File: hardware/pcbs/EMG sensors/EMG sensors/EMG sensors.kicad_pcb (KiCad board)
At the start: 4 copper layers, 65 x 26 mm, 29 parts, among them IC1 INA128, J1 Conn_01x04_Pin, J2 Conn_01x01_Pin, U6 OPA2188AIDR, U7 OPA188AIDR

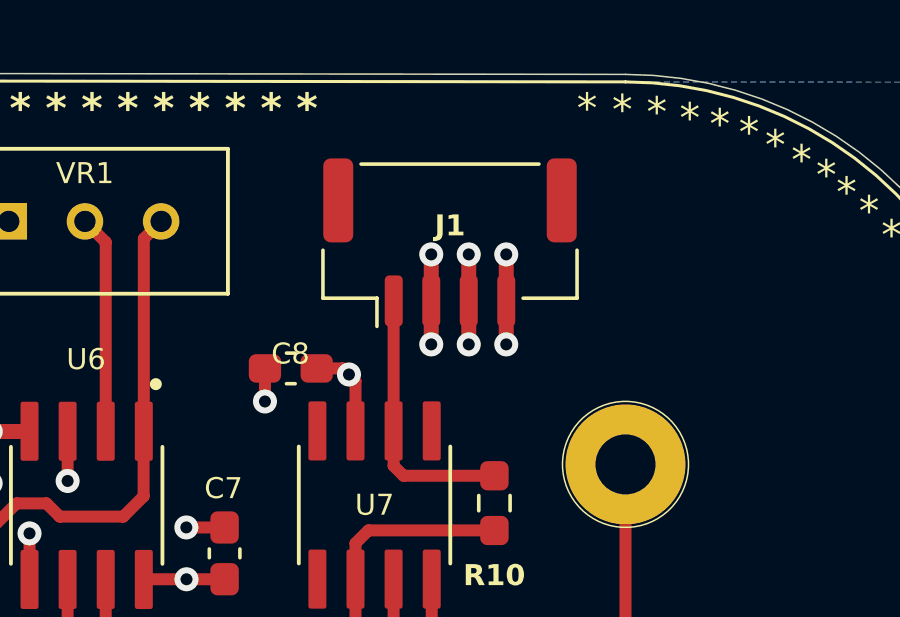
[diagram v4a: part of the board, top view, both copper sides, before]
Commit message: Connector update of the sEMG sensor
Changed it to be JST_GH_SM04B instead of JST_GH_BM04B for easier use
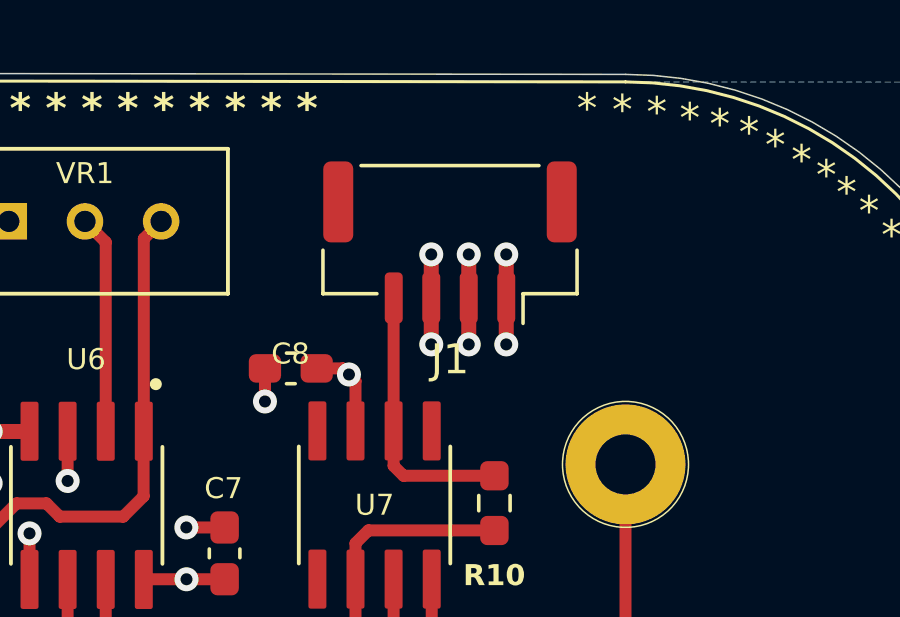
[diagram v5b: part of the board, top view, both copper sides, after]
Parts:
- J1: footprint Connector_JST:JST_GH_BM04B-GHS-TBT_1x04-1MP_P1.25mm_Vertical -> Connector_JST:JST_GH_SM04B-GHS-TB_1x04-1MP_P1.25mm_Horizontal
- turned J1 to 180 degrees
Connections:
- J1 pad 1: /AEMG -> /+5.5V
- J1 pad 2: GND -> /-5.5V
- J1 pad 3: /-5.5V -> GND
- J1 pad 4: /+5.5V -> /AEMG
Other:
- board text added: "v0.3"
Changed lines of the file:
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@@
 		)
 	)
-	(footprint "Connector_JST:JST_GH_BM04B-GHS-TBT_1x04-1MP_P1.25mm_Vertical"
+	(footprint "Connector_JST:JST_GH_SM04B-GHS-TB_1x04-1MP_P1.25mm_Horizontal"
 		(layer "F.Cu")
-		(at 145.15 103.2)
-		(descr "JST GH series connector, BM04B-GHS-TBT (http://www.jst-mfg.com/product/pdf/eng/eGH.pdf), generated with kicad-footprint-generator")
-		(tags "connector JST GH vertical")
+		(at 145.15 103.2 180)
+		(descr "JST GH series connector, SM04B-GHS-TB (http://www.jst-mfg.com/product/pdf/eng/eGH.pdf), generated with kicad-footprint-generator")
+		(tags "connector JST GH horizontal")
 		(property "Reference" "J1"
-			(at 0 -0.55845 180)
+			(at 0 -3.9 0)
 			(layer "F.SilkS")
 			(effects
 				(font
-					(size 0.7 0.7)
-					(thickness 0.12)
-					(bold yes)
+					(size 1 1)
+					(thickness 0.15)
 				)
 			)
 		)
 		(property "Value" "Conn_01x04_Pin"
-			(at 0 4 180)
+			(at 0 3.9 0)
 			(layer "F.Fab")
-			(hide yes)
 			(effects
 				(font
@@
 		)
 		(property "Datasheet" "~"
-			(at 0 0 180)
+			(at 0 0 0)
 			(layer "F.Fab")
 			(hide yes)
@@
 		)
 		(property "Description" "Generic connector, single row, 01x04, script generated"
-			(at 0 0 180)
+			(at 0 0 0)
 			(layer "F.Fab")
 			(hide yes)
@@
 		(attr smd)
 		(fp_line
-			(start -4.235 0.26)
-			(end -4.235 1.86)
+			(start 4.235 -0.26)
+			(end 4.235 -1.71)
 			(stroke
 				(width 0.12)
@@
 		)
 		(fp_line
-			(start -4.235 1.86)
-			(end -2.435 1.86)
+			(start 4.235 -1.71)
+			(end 2.435 -1.71)
 			(stroke
 				(width 0.12)
@@
 		)
 		(fp_line
-			(start -2.965 -2.61)
-			(end 2.965 -2.61)
+			(start -2.435 -1.71)
+			(end -2.435 -2.7)
 			(stroke
 				(width 0.12)
@@
 		)
 		(fp_line
-			(start -2.435 1.86)
-			(end -2.435 2.8)
+			(start -2.965 2.56)
+			(end 2.965 2.56)
 			(stroke
 				(width 0.12)
@@
 		)
 		(fp_line
-			(start 4.235 0.26)
-			(end 4.235 1.86)
+			(start -4.235 -0.26)
+			(end -4.235 -1.71)
 			(stroke
 				(width 0.12)
@@
 		)
 		(fp_line
-			(start 4.235 1.86)
-			(end 2.435 1.86)
+			(start -4.235 -1.71)
+			(end -2.435 -1.71)
 			(stroke
 				(width 0.12)
@@
 		)
 		(fp_line
-			(start -4.73 -3.3)
-			(end -2.72 -3.3)
+			(start 4.73 3.2)
+			(end 2.72 3.2)
 			(stroke
 				(width 0.05)
@@
 		)
 		(fp_line
-			(start -4.73 0.5)
-			(end -4.73 -3.3)
+			(start 4.73 -0.5)
+			(end 4.73 3.2)
 			(stroke
 				(width 0.05)
@@
 		)
 		(fp_line
-			(start -4.63 0.5)
-			(end -4.73 0.5)
+			(start 4.63 -0.5)
+			(end 4.73 -0.5)
 			(stroke
 				(width 0.05)
@@
 		)
 		(fp_line
-			(start -4.63 2.25)
-			(end -4.63 0.5)
+			(start 4.63 -2.1)
+			(end 4.63 -0.5)
 			(stroke
 				(width 0.05)
@@
 		)
 		(fp_line
-			(start -2.72 -3.3)
-			(end -2.72 -3)
+			(start 2.72 3.2)
+			(end 2.72 2.95)
 			(stroke
 				(width 0.05)
@@
 		)
 		(fp_line
-			(start -2.72 -3)
-			(end 2.719999 -3)
+			(start 2.72 2.95)
+			(end -2.72 2.95)
 			(stroke
 				(width 0.05)
@@
 		)
 		(fp_line
-			(start -2.680001 2.25)
-			(end -4.63 2.25)
+			(start 2.68 -2.1)
+			(end 4.63 -2.1)
 			(stroke
 				(width 0.05)
@@
 		)
 		(fp_line
-			(start -2.68 3.3)
-			(end -2.680001 2.25)
+			(start 2.68 -3.2)
+			(end 2.68 -2.1)
 			(stroke
 				(width 0.05)
@@
 		)
 		(fp_line
-			(start 2.68 2.250001)
-			(end 2.68 3.3)
+			(start -2.68 -2.1)
+			(end -2.68 -3.2)
 			(stroke
 				(width 0.05)
@@
 		)
 		(fp_line
-			(start 2.68 3.3)
-			(end -2.68 3.3)
+			(start -2.68 -3.2)
+			(end 2.68 -3.2)
 			(stroke
 				(width 0.05)
@@
 		)
 		(fp_line
-			(start 2.719999 -3)
-			(end 2.72 -3.3)
+			(start -2.72 3.2)
+			(end -4.73 3.2)
 			(stroke
 				(width 0.05)
@@
 		)
 		(fp_line
-			(start 2.72 -3.3)
-			(end 4.73 -3.3)
+			(start -2.72 2.95)
+			(end -2.72 3.2)
 			(stroke
 				(width 0.05)
@@
 		)
 		(fp_line
-			(start 4.629999 0.5)
-			(end 4.63 2.25)
+			(start -4.63 -0.5)
+			(end -4.63 -2.1)
 			(stroke
 				(width 0.05)
@@
 		)
 		(fp_line
-			(start 4.63 2.25)
-			(end 2.68 2.250001)
+			(start -4.63 -2.1)
+			(end -2.68 -2.1)
 			(stroke
 				(width 0.05)
@@
 		)
 		(fp_line
-			(start 4.73 -3.3)
-			(end 4.73 0.5)
+			(start -4.73 3.2)
+			(end -4.73 -0.5)
 			(stroke
 				(width 0.05)
@@
 		)
 		(fp_line
-			(start 4.73 0.5)
-			(end 4.629999 0.5)
+			(start -4.73 -0.5)
+			(end -4.63 -0.5)
 			(stroke
 				(width 0.05)
@@
 		)
 		(fp_line
-			(start -4.125 -2.5)
-			(end 4.125 -2.5)
+			(start 4.125 -1.6)
+			(end 4.125 2.45)
 			(stroke
 				(width 0.1)
@@
 		)
 		(fp_line
-			(start -4.124999 1.75)
-			(end -4.125 -2.5)
+			(start -1.875 -0.892893)
+			(end -1.375 -1.6)
 			(stroke
 				(width 0.1)
@@
 		)
 		(fp_line
-			(start -4.124999 1.75)
-			(end 4.125 1.75)
+			(start -2.375 -1.6)
+			(end -1.875 -0.892893)
 			(stroke
 				(width 0.1)
@@
 		)
 		(fp_line
-			(start -2.375 1.75)
-			(end -1.875 1.042893)
+			(start -4.125 2.45)
+			(end 4.125 2.45)
 			(stroke
 				(width 0.1)
@@
 		)
 		(fp_line
-			(start -1.875 1.042893)
-			(end -1.375 1.75)
+			(start -4.125 -1.6)
+			(end 4.125 -1.6)
 			(stroke
 				(width 0.1)
@@
 		)
 		(fp_line
-			(start 4.125 1.75)
-			(end 4.125 -2.5)
+			(start -4.125 -1.6)
+			(end -4.125 2.45)
 			(stroke
 				(width 0.1)
@@
 			(layer "F.Fab")
 		)
-		(fp_poly
-			(pts
-				(xy -2.125 -0.5) (xy -1.625001 -0.5) (xy -1.625 0) (xy -2.125 0)
-			)
-			(stroke
-				(width 0.1)
-				(type solid)
-			)
-			(fill no)
-			(layer "F.Fab")
-		)
-		(fp_poly
-			(pts
-				(xy -0.875 -0.5) (xy -0.375001 -0.5) (xy -0.375 0) (xy -0.875 0)
-			)
-			(stroke
-				(width 0.1)
-				(type solid)
-			)
-			(fill no)
-			(layer "F.Fab")
-		)
-		(fp_poly
-			(pts
-				(xy 0.375 -0.5) (xy 0.875 -0.500001) (xy 0.875 0) (xy 0.375 0)
-			)
-			(stroke
-				(width 0.1)
-				(type solid)
-			)
-			(fill no)
+		(fp_text user "${REFERENCE}"
+			(at 0 0 0)
 			(layer "F.Fab")
-		)
-		(fp_poly
-			(pts
-				(xy 1.625 -0.5) (xy 2.125 -0.5) (xy 2.125 0) (xy 1.625 0)
-			)
-			(stroke
-				(width 0.1)
-				(type solid)
+			(effects
+				(font
+					(size 1 1)
+					(thickness 0.15)
+				)
 			)
-			(fill no)
-			(layer "F.Fab")
 		)
 		(pad "1" smd roundrect
-			(at -1.875 1.95)
+			(at -1.875 -1.85 180)
 			(size 0.6 1.7)
 			(layers "F.Cu" "F.Mask" "F.Paste")
 			(roundrect_rratio 0.25)
-			(net 12 "/AEMG")
+			(net 11 "/+5.5V")
 			(pinfunction "Pin_1")
 			(pintype "passive")
 		)
 		(pad "2" smd roundrect
-			(at -0.625 1.95)
+			(at -0.625 -1.85 180)
 			(size 0.6 1.7)
 			(layers "F.Cu" "F.Mask" "F.Paste")
 			(roundrect_rratio 0.25)
-			(net 18 "GND")
+			(net 10 "/-5.5V")
 			(pinfunction "Pin_2")
 			(pintype "passive")
 		)
 		(pad "3" smd roundrect
-			(at 0.625 1.95)
+			(at 0.625 -1.85 180)
 			(size 0.6 1.7)
 			(layers "F.Cu" "F.Mask" "F.Paste")
 			(roundrect_rratio 0.25)
-			(net 10 "/-5.5V")
+			(net 18 "GND")
 			(pinfunction "Pin_3")
 			(pintype "passive")
 		)
 		(pad "4" smd roundrect
-			(at 1.875 1.950001)
+			(at 1.875 -1.85 180)
 			(size 0.6 1.7)
 			(layers "F.Cu" "F.Mask" "F.Paste")
 			(roundrect_rratio 0.25)
-			(net 11 "/+5.5V")
+			(net 12 "/AEMG")
 			(pinfunction "Pin_4")
 			(pintype "passive")
 		)
 		(pad "MP" smd roundrect
-			(at -3.725 -1.4)
-			(size 1 2.8)
+			(at -3.725 1.35 180)
+			(size 1 2.7)
 			(layers "F.Cu" "F.Mask" "F.Paste")
 			(roundrect_rratio 0.25)
 		)
 		(pad "MP" smd roundrect
-			(at 3.725 -1.4)
-			(size 1 2.8)
+			(at 3.725 1.35 180)
+			(size 1 2.7)
 			(layers "F.Cu" "F.Mask" "F.Paste")
 			(roundrect_rratio 0.25)
 		)
 		(embedded_fonts no)
-		(model "${KICAD9_3DMODEL_DIR}/Connector_JST.3dshapes/JST_GH_BM04B-GHS-TBT_1x04-1MP_P1.25mm_Vertical.step"
+		(model "${KICAD9_3DMODEL_DIR}/Connector_JST.3dshapes/JST_GH_SM04B-GHS-TB_1x04-1MP_P1.25mm_Horizontal.step"
 			(offset
 				(xyz 0 0 0)
@@
 	)
 	(gr_text "SensaLimb sEMG"
-		(at 141.1 101.61475 0)
+		(at 141.1 101 0)
+		(layer "B.SilkS")
+		(effects
+			(font
+				(size 1.5 1.5)
+				(thickness 0.3)
+				(bold yes)
+			)
+			(justify left bottom mirror)
+		)
+	)
+	(gr_text "v0.3\n"
+		(at 134.2 121.6 0)
 		(layer "B.SilkS")
 		(effects
@@
 	)
 	(segment
-		(start 143.27 105.155)
-		(end 143.275 105.15)
+		(start 143.30695 109.44675)
+		(end 143.27 109.4837)
 		(width 0.4)
 		(layer "F.Cu")
@@
 	)
 	(segment
-		(start 143.30695 109.44675)
-		(end 143.27 109.4837)
+		(start 143.27 105.055)
+		(end 143.275 105.05)
 		(width 0.4)
 		(layer "F.Cu")
@@
 	(segment
 		(start 143.27 109.4837)
-		(end 143.27 105.155)
+		(end 143.27 105.055)
 		(width 0.4)
 		(layer "F.Cu")
@@
 		(width 0.4)
 		(layer "F.Cu")
-		(net 12)
-	)
-	(segment
-		(start 143.27 105.1965)
-		(end 143.23195 105.15845)
-		(width 0.4)
-		(layer "F.Cu")

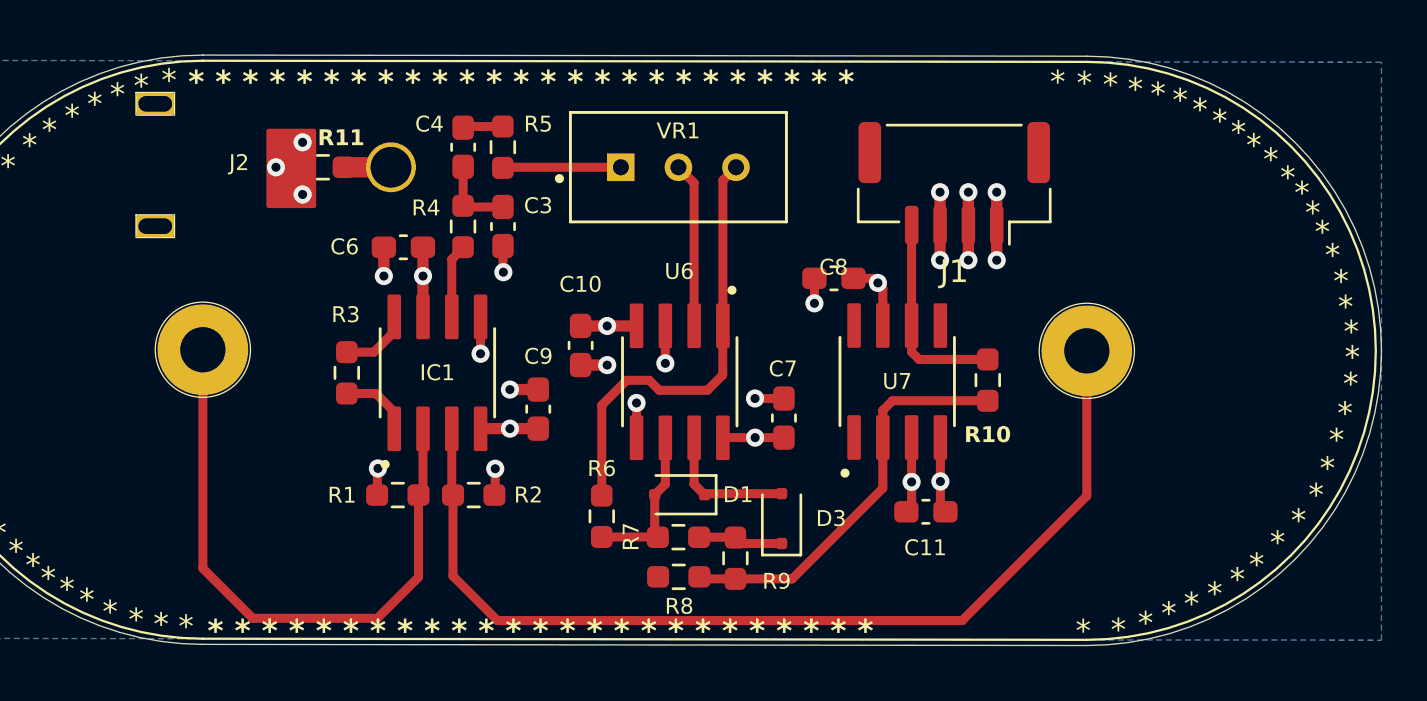
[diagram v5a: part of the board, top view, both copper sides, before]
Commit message: ADC + sEMG changes
sEMG - connector updates
ADC - major changes - connectors, layout changes
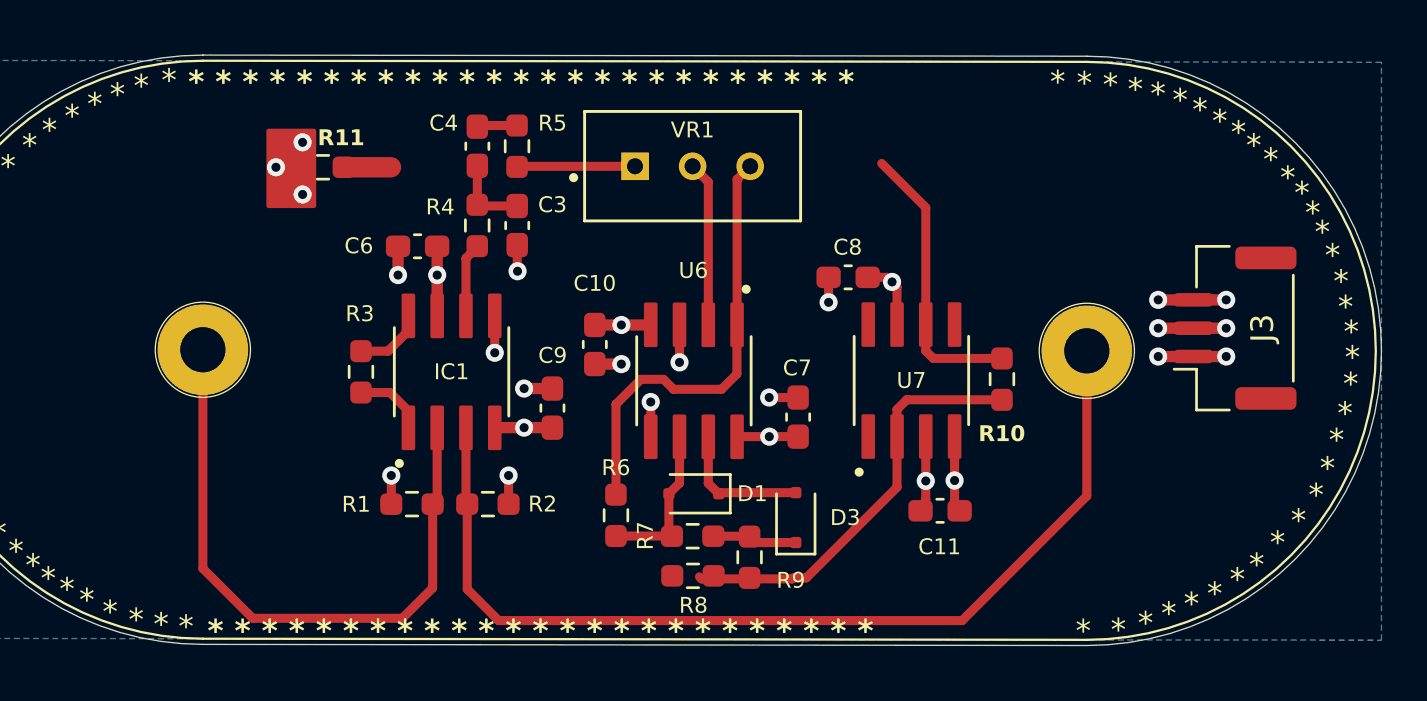
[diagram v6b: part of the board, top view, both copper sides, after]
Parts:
- removed J1: Conn_01x04_Pin, Connector_JST:JST_GH_SM04B-GHS-TB_1x04-1MP_P1.25mm_Horizontal
- removed J2: Conn_01x01_Pin, Connectors:DIN_Male_1PIN_1.5mm
- added J3: Conn_01x03_Pin, Connector_JST:JST_GH_SM03B-GHS-TB_1x03-1MP_P1.25mm_Horizontal, F.Cu at (157.6, 109.6)
- moved R1 0.74 mm to (121.2, 117.4)
- moved R2 0.74 mm to (124.6, 117.4)
- moved C7 0.63 mm to (138.3, 113.5)
- moved R8 0.63 mm to (133.6, 120.5)
- moved R9 0.63 mm to (136.1, 119.7)
- moved U7 0.63 mm to (143.3, 111.9)
- moved IC1 0.63 mm to (123.0, 111.5)
- moved R3 0.63 mm to (119.0, 111.5)
- moved C3 0.63 mm to (125.9, 105.1)
- moved C6 0.63 mm to (121.5, 106.0)
- moved C9 0.63 mm to (127.4, 113.1)
- moved C10 0.63 mm to (129.3, 110.3)
- moved C11 0.63 mm to (144.5, 117.7)
- moved C4 0.63 mm to (124.1, 101.6)
- moved C8 0.63 mm to (140.5, 107.4)
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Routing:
- net /AEMG: track 9.33 -> 12.7 mm
- net Vin1: track 25.8 -> 26.7 mm

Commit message: BMS v0.3 + main folder reconstruction
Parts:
- added J2: Conn_01x01_Pin, Connectors:DIN_Male_1PIN_1.5mm, F.Cu at (110.5, 103.6)
- added J4: Conn_01x01_Pin, Connectors:DIN_Male_1PIN_1.5mm, F.Cu at (151.7, 101.2)
- moved R11 4.69 mm to (116.4, 107.1), turned to 90 degrees
- moved J3 1.00 mm to (158.3, 110.2)
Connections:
- C10 pad 2: Ref -> GND
- C11 pad 2: Ref -> GND
- C3 pad 2: Ref -> GND
- C6 pad 2: Ref -> GND
- C7 pad 2: Ref -> GND
- C8 pad 2: Ref -> GND
- C9 pad 2: Ref -> GND
- IC1 pad 5: Ref -> GND
- R1 pad 1: Ref -> GND
- R11 pad 2: Ref -> Net-(J2-Pin_1)
- R2 pad 2: Ref -> GND
- U6 pad 3: Ref -> GND
- U6 pad 5: Ref -> GND
- U7 pad 3: Ref -> GND
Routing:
- net Ref: track 20.3 -> 0.00 mm, vias 12 -> 0
- net GND: track 3.00 -> 21.3 mm, vias 5 -> 17
- net INVERTED: track 19.6 -> 26.8 mm
- net Net-(J2-Pin_1): track 0.00 -> 6.71 mm
- net Net-(U6--INA): track 12.6 -> 15.2 mm
- net Net-(U7--IN): track 18.7 -> 18.0 mm
- added copper zone on In1.Cu, net GND
- removed copper zone on In1.Cu, net Ref
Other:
- board text added: "v0.4"
- board text removed: "v0.3"
